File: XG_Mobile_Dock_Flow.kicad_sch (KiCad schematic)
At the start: 72 parts, among them J1 5-1775443-8, J13 39300240, J14 469911008, J17 8730, J2 20455-040E-76, J3 20455-040E-76, J4 3-2362375-4, J5 USB_C_Receptacle, SW1 SW_Push, U1 DS160PR410RNQR, U2 DS160PR410RNQR

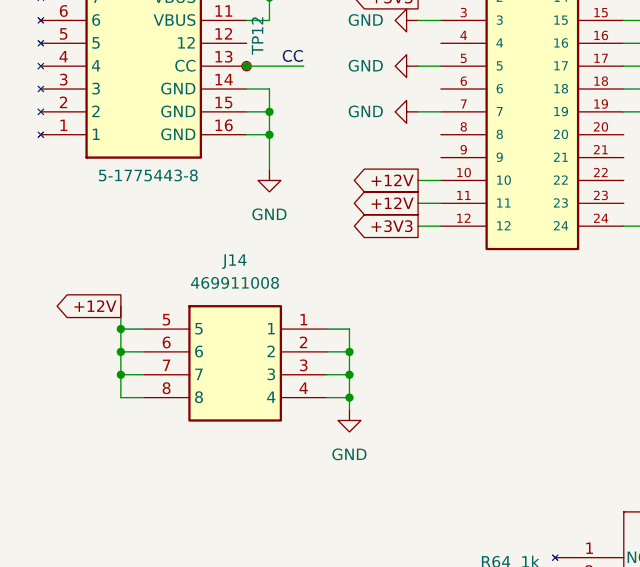
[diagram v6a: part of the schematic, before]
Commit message: fixed pcie 8 power connector part number
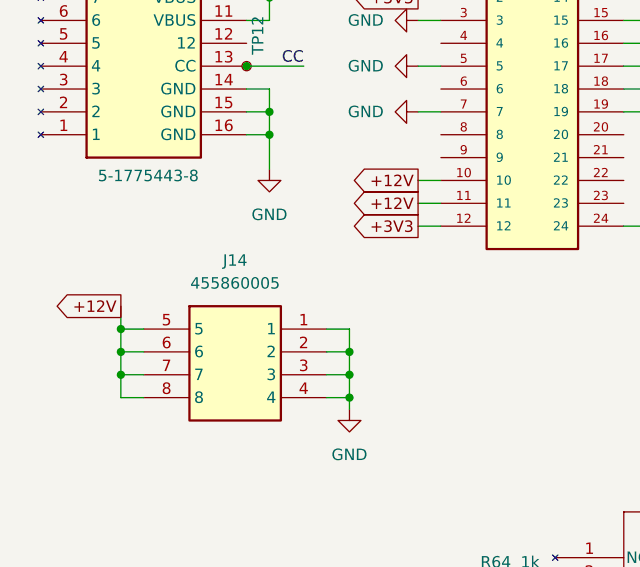
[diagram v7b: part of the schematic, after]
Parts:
- J14: value 469911008 -> 455860005; LCSC C17470577 -> C17693884; Part_Number 469911008 -> 455860005
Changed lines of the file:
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@@
 			)
 		)
-		(property "Value" "469911008"
+		(property "Value" "455860005"
 			(at 36.83 170.18 0)
 			(effects
@@
 			)
 		)
-		(property "Part_Number" "469911008"
+		(property "Part_Number" "455860005"
 			(at 26.67 175.26 0)
 			(effects
@@
 			)
 		)
-		(property "LCSC" "C17470577"
+		(property "LCSC" "C17693884"
 			(at 26.67 175.26 0)
 			(effects

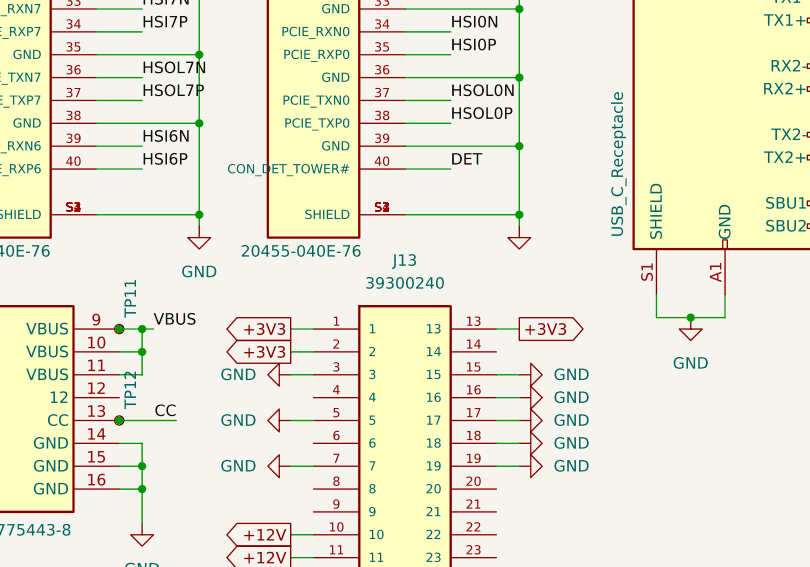
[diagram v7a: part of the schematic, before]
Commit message: updated part number for molex with latest one
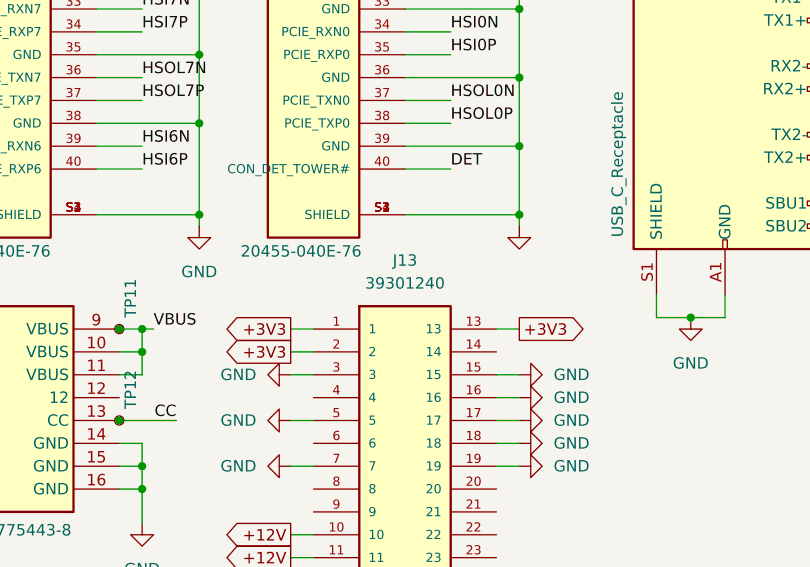
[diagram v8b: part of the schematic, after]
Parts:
- J13: value 39300240 -> 39301240; LCSC C492361 -> C492347; Part_Number 39300240 -> 39301240
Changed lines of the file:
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@@
 			)
 		)
-		(property "Value" "39300240"
+		(property "Value" "39301240"
 			(at 69.85 130.81 0)
 			(effects
@@
 			)
 		)
-		(property "Part_Number" "39300240"
+		(property "Part_Number" "39301240"
 			(at 69.85 148.59 0)
 			(effects
@@
 			)
 		)
-		(property "LCSC" "C492361"
+		(property "LCSC" "C492347"
 			(at 69.85 148.59 0)
 			(effects
